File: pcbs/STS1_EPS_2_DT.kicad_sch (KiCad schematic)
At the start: 19 parts, among them Q2 SI7272DP-T1-GE3, Q3 2N7002, Q4 2N7002, U1 4072, U2 LTC6995IDCB-1

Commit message: Changed some footprints that had the wrong shape in EPS 2.1.
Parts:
- U1: footprint Package_SO:SOIC-14_3.9x8.7mm_P1.27mm -> STS_Misc:SOP127P780X200-14N
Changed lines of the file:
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@@
 			)
 		)
-		(property "Footprint" "Package_SO:SOIC-14_3.9x8.7mm_P1.27mm"
+		(property "Footprint" "STS_Misc:SOP127P780X200-14N"
 			(at 119.38 95.25 0)
 			(effects
@@
 			)
 		)
-		(property "Footprint" "Package_SO:SOIC-14_3.9x8.7mm_P1.27mm"
+		(property "Footprint" "STS_Misc:SOP127P780X200-14N"
 			(at 119.38 39.37 0)
 			(effects

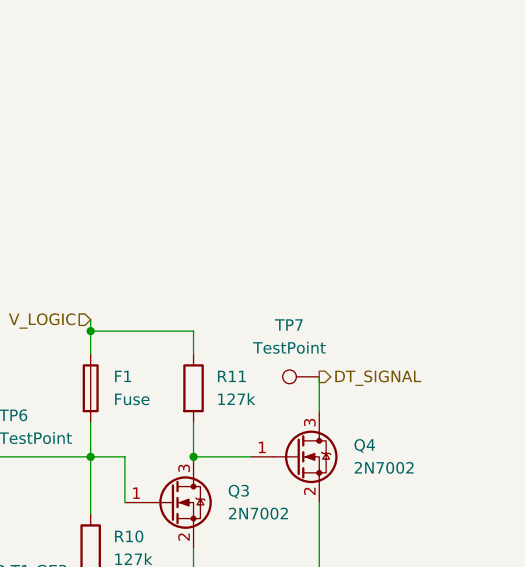
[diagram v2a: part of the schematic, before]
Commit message: Signals to the bus gate should now be provided with supply voltage the proper way.
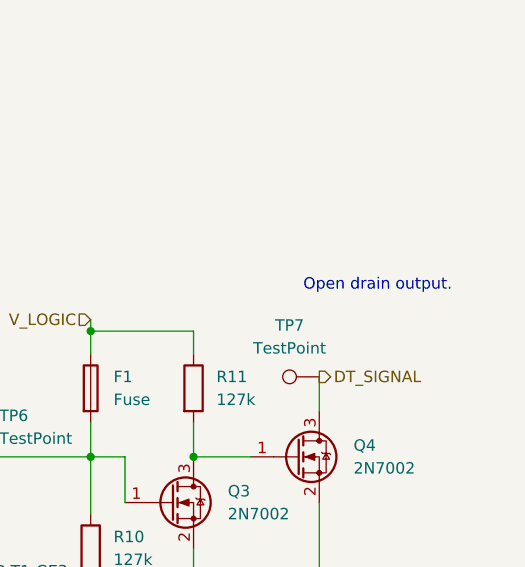
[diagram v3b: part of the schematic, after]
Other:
- note added: "Open drain output."
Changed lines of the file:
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@@
+		)
+	)
+	(text "Open drain output."
+		(exclude_from_sim no)
+		(at 264.922 64.262 0)
+		(effects
+			(font
+				(size 1.27 1.27)
+			)
+			(justify left bottom)
 		)
 	)

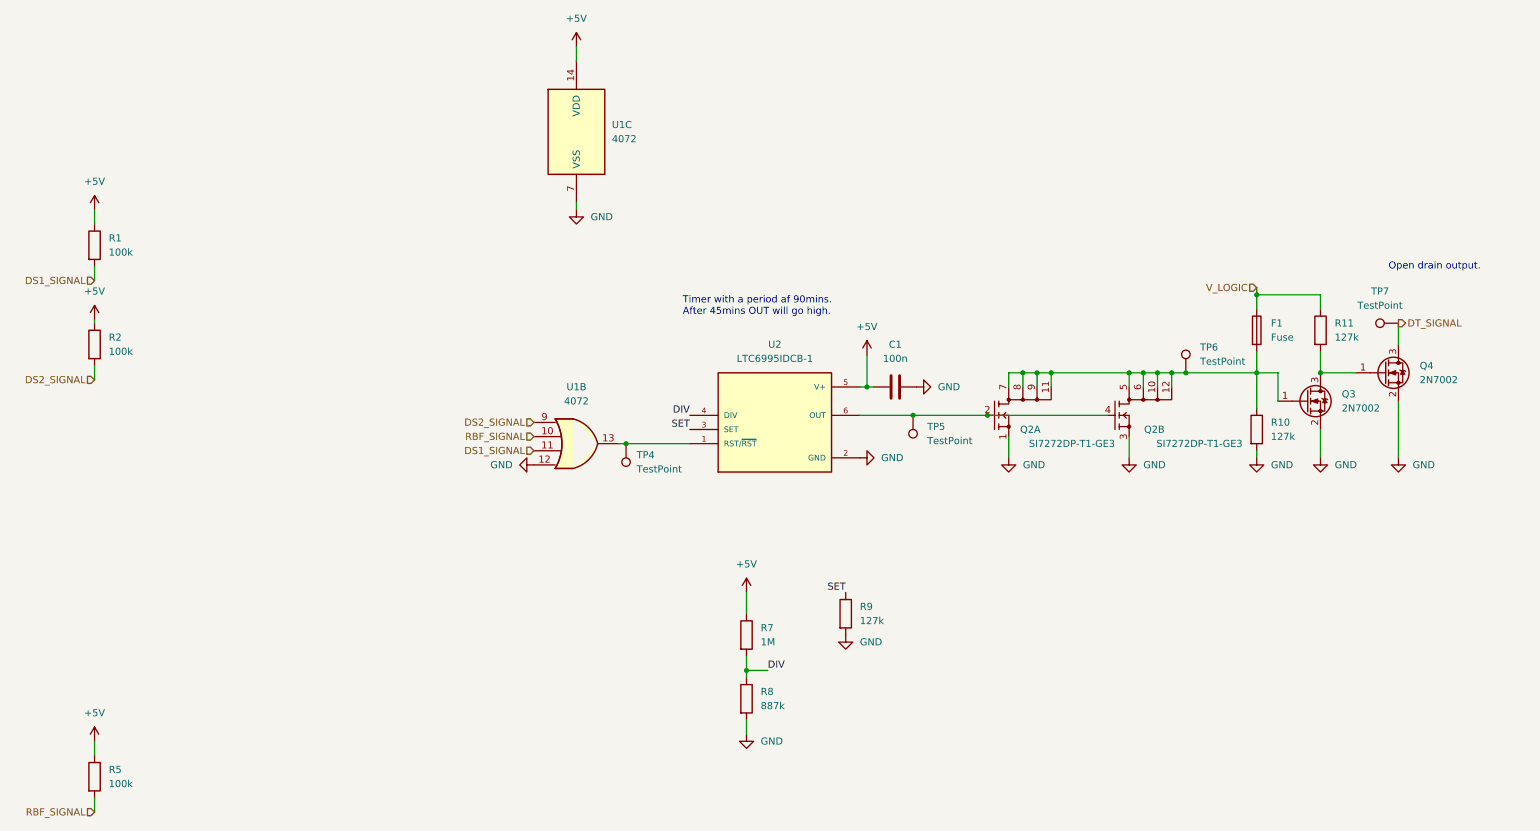
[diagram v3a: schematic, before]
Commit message: Added possibilities to short single interrupt sources.
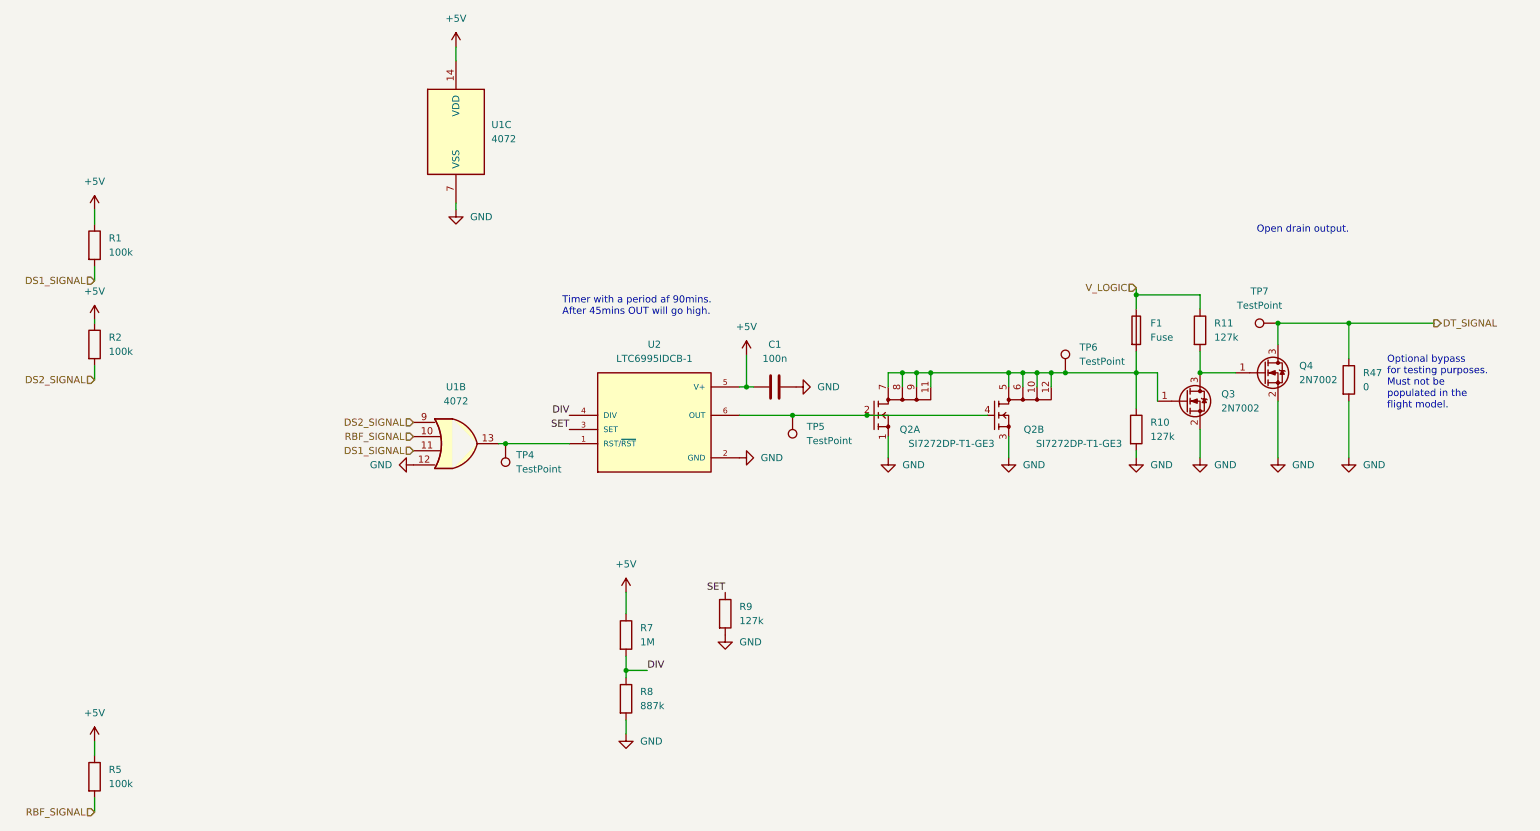
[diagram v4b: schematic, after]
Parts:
- added R47: 0, Resistor_SMD:R_0805_2012Metric, symbol Device:R
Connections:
- net DT_SIGNAL: now also R47.1
- net GND: now also R47.2
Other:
- note added: "Optional bypass for testing purposes. Must not be populated in the flight model."
- moved on the sheet: C1, F1, Q2A, Q2B, Q3, Q4, R10, R11, R7, R8, R9, TP4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

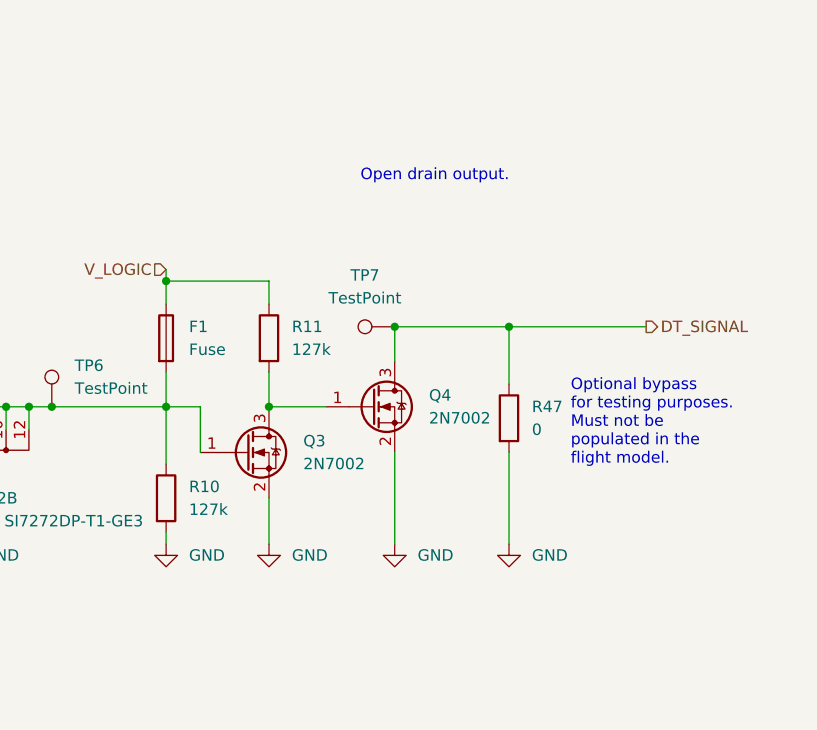
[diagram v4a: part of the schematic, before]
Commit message: Fixed the logic behing the GATE_SIGNAL signal.
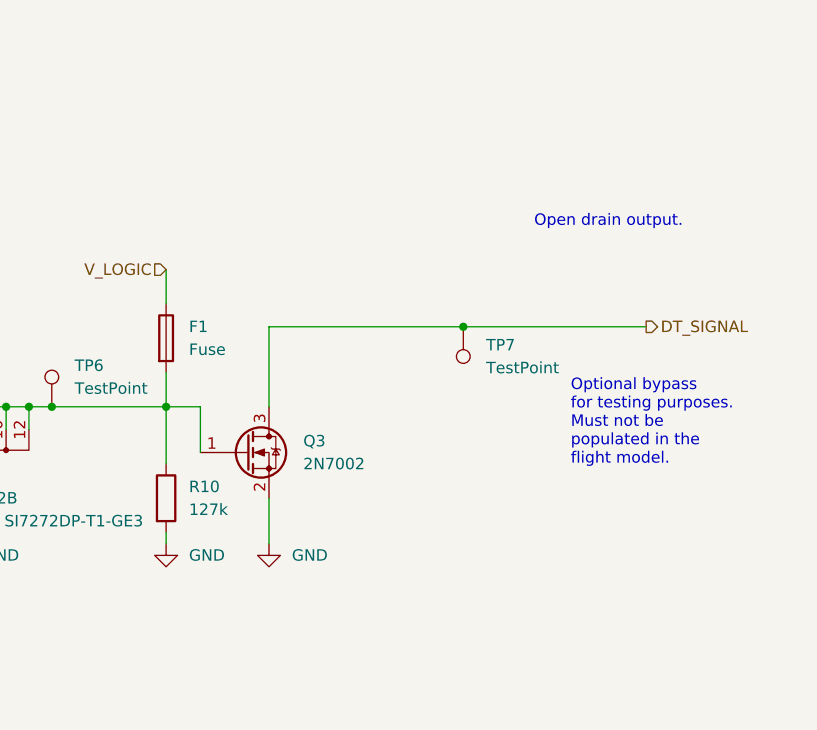
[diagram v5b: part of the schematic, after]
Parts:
- removed Q4: 2N7002, Package_TO_SOT_SMD:SOT-23, symbol Transistor_FET:2N7002
- removed R11: 127k, Resistor_SMD:R_0805_2012Metric, symbol Device:R
- removed R47: 0, Resistor_SMD:R_0805_2012Metric, symbol Device:R
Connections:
- net DT_SIGNAL: now also Q3.3 (D)
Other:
- moved on the sheet: TP7

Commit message: Intermediate commit.
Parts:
- U1: footprint STS_Misc:SOP127P780X200-14N -> Package_SO:SOIC-14_3.9x8.7mm_P1.27mm
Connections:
- net +5V: no longer C1.1, R1.1, R2.1, R5.1, U1.14 (VDD), U2.5 (V+)
- net V_LOGIC: now also C1.1, R1.1, R2.1, R5.1, U1.14 (VDD), U2.5 (V+)
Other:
- moved on the sheet: TP5

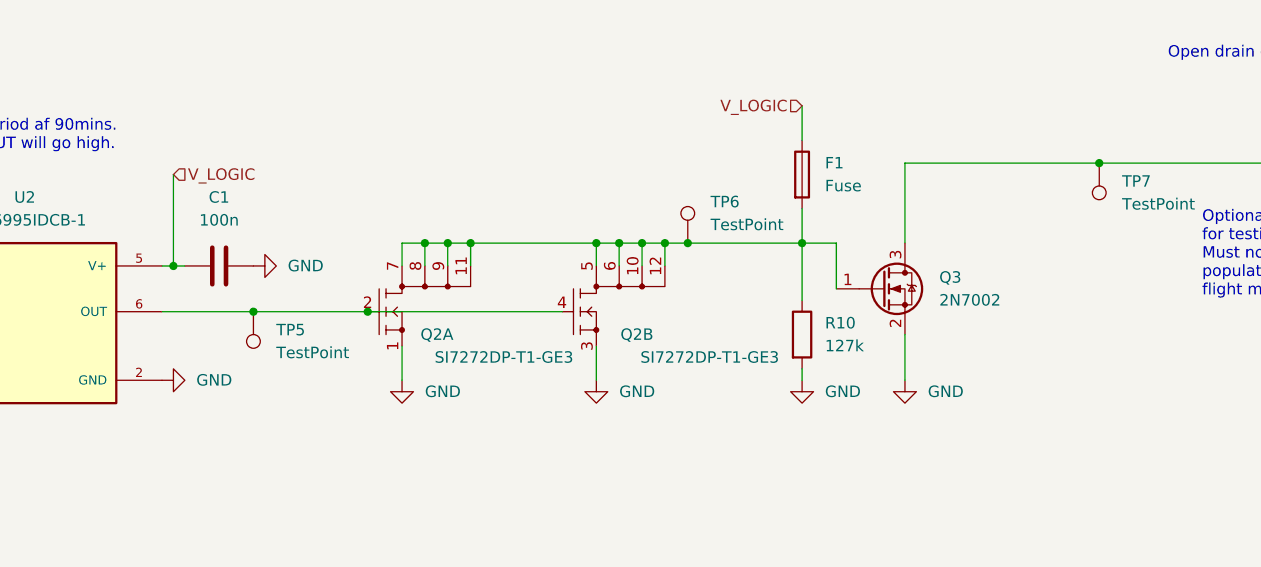
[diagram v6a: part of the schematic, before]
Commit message: Removed UCI connector from STS1_EPS_2 and merged UCI connector with J5 on STS1_EPS_1.
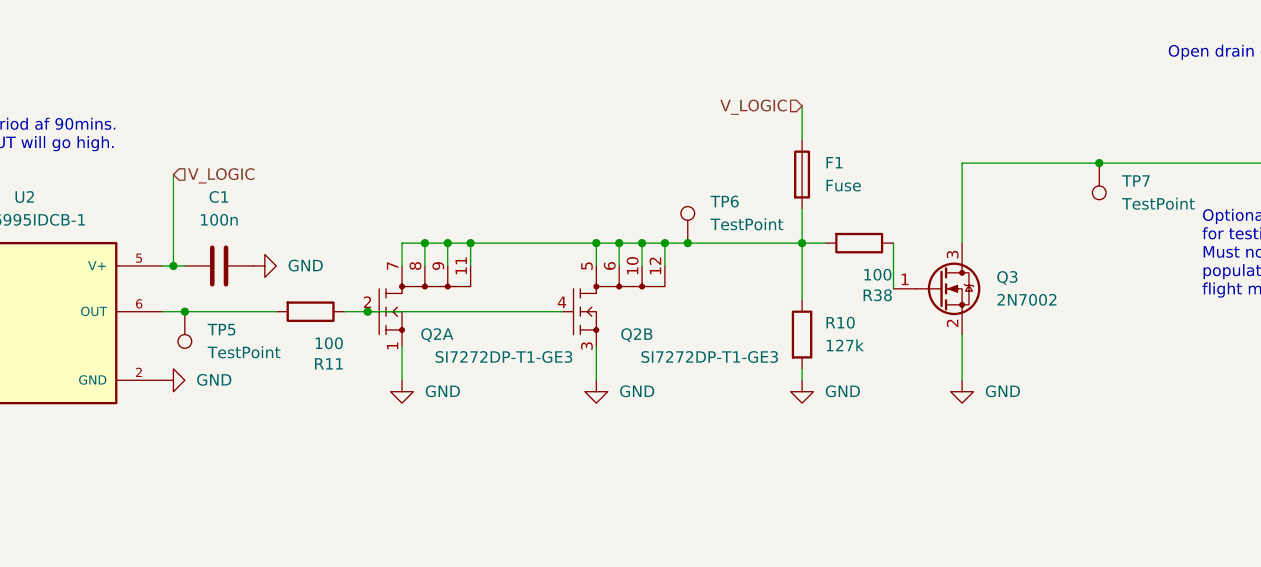
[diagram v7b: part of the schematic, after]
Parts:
- added R11, R38: 100, Resistor_SMD:R_0805_2012Metric, symbol Device:R
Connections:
- net at TP5.1, U2.6 (OUT): now also R11.2; no longer Q2.2 (G1), Q2.4 (G2)
- net at F1.2, Q2.10 (D2_3), Q2.11 (D1_4)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: now also R38.2; no longer Q3.1 (G)
- new net: Q2.2 (G1), Q2.4 (G2), R11.1
- new net: Q3.1 (G), R38.1
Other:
- moved on the sheet: Q3, TP5
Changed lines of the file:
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@@
+	)
+	(junction
+		(at 151.13 90.17)
+		(diameter 0)
+		(color 0 0 0 0)
 	)
 	(junction
@@
 		(color 0 0 0 0)
 	)
-	(junction
-		(at 158.75 90.17)
-		(diameter 0)
-		(color 0 0 0 0)
-	)
 	(wire
 		(pts
@@
 	(wire
 		(pts
+			(xy 168.91 90.17) (xy 171.45 90.17)
+		)
+		(stroke
+			(width 0)
+			(type default)
+		)
+	)
+	(wire
+		(pts
 			(xy 148.59 85.09) (xy 149.86 85.09)
 		)
@@
 	(wire
 		(pts
-			(xy 231.14 97.79) (xy 231.14 92.71)
-		)
-		(stroke
-			(width 0)
-			(type default)
-		)
-	)
-	(wire
-		(pts
 			(xy 175.26 93.98) (xy 175.26 97.79)
 		)
@@
 	(wire
 		(pts
-			(xy 231.14 82.55) (xy 231.14 73.66)
+			(xy 237.49 82.55) (xy 237.49 73.66)
 		)
 		(stroke
@@
 	(wire
 		(pts
-			(xy 148.59 90.17) (xy 158.75 90.17)
+			(xy 148.59 90.17) (xy 151.13 90.17)
 		)
 		(stroke
@@
 	(wire
 		(pts
-			(xy 223.52 82.55) (xy 223.52 87.63)
+			(xy 151.13 90.17) (xy 161.29 90.17)
+		)
+		(stroke
+			(width 0)
+			(type default)
+		)
+	)
+	(wire
+		(pts
+			(xy 229.87 82.55) (xy 229.87 87.63)
 		)
 		(stroke
@@
 	(wire
 		(pts
-			(xy 158.75 90.17) (xy 171.45 90.17)
-		)
-		(stroke
-			(width 0)
-			(type default)
-		)
-	)
-	(wire
-		(pts
 			(xy 33.02 69.85) (xy 33.02 73.66)
 		)
@@
 	(wire
 		(pts
-			(xy 219.71 82.55) (xy 223.52 82.55)
-		)
-		(stroke
-			(width 0)
-			(type default)
-		)
-	)
-	(wire
-		(pts
-			(xy 231.14 73.66) (xy 252.73 73.66)
+			(xy 219.71 82.55) (xy 222.25 82.55)
+		)
+		(stroke
+			(width 0)
+			(type default)
+		)
+	)
+	(wire
+		(pts
+			(xy 237.49 73.66) (xy 252.73 73.66)
+		)
+		(stroke
+			(width 0)
+			(type default)
+		)
+	)
+	(wire
+		(pts
+			(xy 237.49 92.71) (xy 237.49 97.79)
 		)
 		(stroke
@@
 	(symbol
 		(lib_id "Connector:TestPoint")
-		(at 158.75 90.17 180)
+		(at 151.13 90.17 180)
 		(unit 1)
 		(exclude_from_sim no)
@@
 		(fields_autoplaced yes)
 		(property "Reference" "TP5"
-			(at 161.29 92.2019 0)
+			(at 153.67 92.2019 0)
 			(effects
 				(font
@@
 		)
 		(property "Value" "TestPoint"
-			(at 161.29 94.7419 0)
+			(at 153.67 94.7419 0)
 			(effects
 				(font
@@
 		)
 		(property "Footprint" "TestPoint:TestPoint_THTPad_D1.0mm_Drill0.5mm"
-			(at 153.67 90.17 0)
+			(at 146.05 90.17 0)
 			(effects
 				(font
@@
 		)
 		(property "Datasheet" "~"
-			(at 153.67 90.17 0)
-			(effects
-				(font
-					(size 1.27 1.27)
-				)
-				(hide yes)
-			)
-		)
-		(property "Description" ""
-			(at 158.75 90.17 0)
+			(at 146.05 90.17 0)
+			(effects
+				(font
+					(size 1.27 1.27)
+				)
+				(hide yes)
+			)
+		)
+		(property "Description" ""
+			(at 151.13 90.17 0)
 			(effects
 				(font
@@
 	)
 	(symbol
+		(lib_id "Device:R")
+		(at 226.06 82.55 270)
+		(unit 1)
+		(exclude_from_sim no)
+		(in_bom yes)
+		(on_board yes)
+		(dnp no)
+		(property "Reference" "R38"
+			(at 228.092 88.392 90)
+			(effects
+				(font
+					(size 1.27 1.27)
+				)
+			)
+		)
+		(property "Value" "100"
+			(at 228.092 86.106 90)
+			(effects
+				(font
+					(size 1.27 1.27)
+				)
+			)
+		)
+		(property "Footprint" "Resistor_SMD:R_0805_2012Metric"
+			(at 226.06 80.772 90)
+			(effects
+				(font
+					(size 1.27 1.27)
+				)
+				(hide yes)
+			)
+		)
+		(property "Datasheet" "~"
+			(at 226.06 82.55 0)
+			(effects
+				(font
+					(size 1.27 1.27)
+				)
+				(hide yes)
+			)
+		)
+		(property "Description" ""
+			(at 226.06 82.55 0)
+			(effects
+				(font
+					(size 1.27 1.27)
+				)
+				(hide yes)
+			)
+		)
+		(pin "1"
+		)
+		(pin "2"
+		)
+		(instances
+			(project "STS1_EPS_2"
+				(path "/38c03ff7-ea47-4d00-b37d-ddcaa7d87722/d08cc104-26df-403e-aeed-bb3c2e21e328"
+					(reference "R38")
+					(unit 1)
+				)
+			)
+		)
+	)
+	(symbol
 		(lib_id "power:GND")
 		(at 219.71 97.79 0)
@@
 	)
 	(symbol
+		(lib_id "Device:R")
+		(at 165.1 90.17 270)
+		(unit 1)
+		(exclude_from_sim no)
+		(in_bom yes)
+		(on_board yes)
+		(dnp no)
+		(property "Reference" "R11"
+			(at 167.132 96.012 90)
+			(effects
+				(font
+					(size 1.27 1.27)
+				)
+			)
+		)
+		(property "Value" "100"
+			(at 167.132 93.726 90)
+			(effects
+				(font
+					(size 1.27 1.27)
+				)
+			)
+		)
+		(property "Footprint" "Resistor_SMD:R_0805_2012Metric"
+			(at 165.1 88.392 90)
+			(effects
+				(font
+					(size 1.27 1.27)
+				)
+				(hide yes)
+			)
+		)
+		(property "Datasheet" "~"
+			(at 165.1 90.17 0)
+			(effects
+				(font
+					(size 1.27 1.27)
+				)
+				(hide yes)
+			)
+		)
+		(property "Description" ""
+			(at 165.1 90.17 0)
+			(effects
+				(font
+					(size 1.27 1.27)
+				)
+				(hide yes)
+			)
+		)
+		(pin "1"
+		)
+		(pin "2"
+		)
+		(instances
+			(project "STS1_EPS_2"
+				(path "/38c03ff7-ea47-4d00-b37d-ddcaa7d87722/d08cc104-26df-403e-aeed-bb3c2e21e328"
+					(reference "R11")
+					(unit 1)
+				)
+			)
+		)
+	)
+	(symbol
 		(lib_id "Device:Fuse")
 		(at 219.71 74.93 0)
@@
 	(symbol
 		(lib_id "Transistor_FET:2N7002")
-		(at 228.6 87.63 0)
+		(at 234.95 87.63 0)
 		(unit 1)
 		(exclude_from_sim no)
@@
 		(fields_autoplaced yes)
 		(property "Reference" "Q3"
-			(at 234.95 86.3599 0)
+			(at 241.3 86.3599 0)
 			(effects
 				(font
@@
 		)
 		(property "Value" "2N7002"
-			(at 234.95 88.8999 0)
+			(at 241.3 88.8999 0)
 			(effects
 				(font
@@
 		)
 		(property "Footprint" "Package_TO_SOT_SMD:SOT-23"
-			(at 233.68 89.535 0)
+			(at 240.03 89.535 0)
 			(effects
 				(font
@@
 		)
 		(property "Datasheet" "https://www.onsemi.com/pub/Collateral/NDS7002A-D.PDF"
-			(at 228.6 87.63 0)
-			(effects
-				(font
-					(size 1.27 1.27)
-				)
-				(justify left)
-				(hide yes)
-			)
-		)
-		(property "Description" ""
-			(at 228.6 87.63 0)
+			(at 234.95 87.63 0)
+			(effects
+				(font
+					(size 1.27 1.27)
+				)
+				(justify left)
+				(hide yes)
+			)
+		)
+		(property "Description" ""
+			(at 234.95 87.63 0)
 			(effects
 				(font
@@
 	(symbol
 		(lib_id "power:GND")
-		(at 231.14 97.79 0)
+		(at 237.49 97.79 0)
 		(unit 1)
 		(exclude_from_sim no)
@@
 		(fields_autoplaced yes)
 		(property "Reference" "#PWR034"
-			(at 231.14 104.14 0)
+			(at 237.49 104.14 0)
 			(effects
 				(font
@@
 		)
 		(property "Value" "GND"
-			(at 233.68 99.0599 0)
+			(at 240.03 99.0599 0)
 			(effects
 				(font
@@
 		)
 		(property "Footprint" ""
-			(at 231.14 97.79 0)
+			(at 237.49 97.79 0)
 			(effects
 				(font
@@
 		)
 		(property "Datasheet" ""
-			(at 231.14 97.79 0)
-			(effects
-				(font
-					(size 1.27 1.27)
-				)
-				(hide yes)
-			)
-		)
-		(property "Description" ""
-			(at 231.14 97.79 0)
-			(effects
-				(font
+			(at 237.49 97.79 0)
+			(effects
+				(font
+					(size 1.27 1.27)
+				)
+				(hide yes)
+			)
+		)
+		(property "Description" ""
+			(at 237.49 97.79 0)
+			(effects
+				(font
